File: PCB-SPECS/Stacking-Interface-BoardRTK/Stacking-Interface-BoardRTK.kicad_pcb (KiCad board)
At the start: 2 copper layers, 57 x 93 mm, 15 parts

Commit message: Really trying to get the PCB okay... will have to work on it tmr
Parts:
- RTK_Bottom_Left1: moved to B.Cu
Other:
- board size 57 x 93 mm -> 65 x 96 mm
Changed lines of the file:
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@@
 	)
 	(footprint "Connector_PinHeader_2.54mm:PinHeader_1x10_P2.54mm_Vertical"
-		(layer "F.Cu")
+		(layer "B.Cu")
 		(at 12 25.5 180)
 		(descr "Through hole straight pin header, 1x10, 2.54mm pitch, single row")
 		(tags "Through hole pin header THT 1x10 2.54mm single row")
 		(property "Reference" "RTK_Bottom_Left1"
-			(at 0 2.38 0)
-			(layer "B.SilkS")
+			(at 0 -2.38 0)
+			(layer "F.SilkS")
 			(effects
 				(font
-					(size 1 1)
-					(thickness 0.15)
+					(size 0.6 0.6)
+					(thickness 0.1)
 				)
-				(justify mirror)
 			)
 		)
 		(property "Value" "Conn_01x10_Pin"
-			(at 0 -25.24 0)
-			(layer "B.Fab")
+			(at 0 25.24 0)
+			(layer "F.Fab")
 			(effects
 				(font
@@
 					(thickness 0.15)
 				)
-				(justify mirror)
 			)
 		)
 		(property "Datasheet" "~"
 			(at 0 0 0)
-			(layer "B.Fab")
+			(layer "F.Fab")
 			(hide yes)
 			(effects
@@
 					(thickness 0.15)
 				)
-				(justify mirror)
 			)
 		)
 		(property "Description" "Generic connector, single row, 01x10, script generated"
 			(at 0 0 0)
-			(layer "B.Fab")
+			(layer "F.Fab")
 			(hide yes)
 			(effects
@@
 					(thickness 0.15)
 				)
-				(justify mirror)
 			)
 		)
@@
 				(type solid)
 			)
-			(layer "B.SilkS")
+			(layer "F.SilkS")
 		)
 		(fp_line
@@
 				(type solid)
 			)
-			(layer "B.SilkS")
+			(layer "F.SilkS")
 		)
 		(fp_line
@@
 				(type solid)
 			)
-			(layer "B.SilkS")
+			(layer "F.SilkS")
 		)
 		(fp_line
@@
 				(type solid)
 			)
-			(layer "B.SilkS")
+			(layer "F.SilkS")
 		)
 		(fp_line
@@
 				(type solid)
 			)
-			(layer "B.SilkS")
+			(layer "F.SilkS")
 		)
 		(fp_line
@@
 				(type solid)
 			)
-			(layer "B.SilkS")
+			(layer "F.SilkS")
 		)
 		(fp_line
@@
 				(type solid)
 			)
-			(layer "B.CrtYd")
+			(layer "F.CrtYd")
 		)
 		(fp_line
@@
 				(type solid)
 			)
-			(layer "B.CrtYd")
+			(layer "F.CrtYd")
 		)
 		(fp_line
@@
 				(type solid)
 			)
-			(layer "B.CrtYd")
+			(layer "F.CrtYd")
 		)
 		(fp_line
@@
 				(type solid)
 			)
-			(layer "B.CrtYd")
+			(layer "F.CrtYd")
 		)
 		(fp_line
@@
 		(model "${KICAD9_3DMODEL_DIR}/Connector_PinHeader_2.54mm.3dshapes/PinHeader_1x10_P2.54mm_Vertical.step"
 			(offset
-				(xyz 0 0 0)
+				(xyz 0 11.43 0)
 			)
 			(scale
@@
 			)
 			(rotate
-				(xyz 0 0 0)
+				(xyz 0 0 180)
 			)
 		)
@@
 		(tags "Through hole pin header THT 1x06 2.54mm single row")
 		(property "Reference" "RTK_Top_Right1"
-			(at 0 -2.38 0)
+			(at -14 -2.38 0)
 			(layer "F.SilkS")
 			(effects
 				(font
-					(size 1 1)
-					(thickness 0.15)
+					(size 0.6 0.6)
+					(thickness 0.1)
 				)
+				(justify right)
 			)
 		)
@@
 		(model "${KICAD9_3DMODEL_DIR}/Connector_PinHeader_2.54mm.3dshapes/PinHeader_1x06_P2.54mm_Vertical.step"
 			(offset
-				(xyz 0 0 0)
+				(xyz 0 0 -1.6)
 			)
 			(scale
@@
 			(effects
 				(font
-					(size 1 1)
-					(thickness 0.15)
+					(size 0.6 0.6)
+					(thickness 0.1)
 				)
 			)
@@
 		(model "${KICAD9_3DMODEL_DIR}/Connector_PinHeader_2.54mm.3dshapes/PinHeader_1x08_P2.54mm_Vertical.step"
 			(offset
-				(xyz 0 0 0)
+				(xyz 0 0 -1.6)
 			)
 			(scale
@@
 		(tags "Through hole pin header THT 1x08 2.54mm single row")
 		(property "Reference" "RTK_Bottom_Right1"
-			(at 0 -2.38 0)
+			(at -14 -2.38 0)
 			(layer "F.SilkS")
 			(effects
 				(font
-					(size 1 1)
-					(thickness 0.15)
+					(size 0.6 0.6)
+					(thickness 0.1)
 				)
+				(justify right)
 			)
 		)
@@
 		(model "${KICAD9_3DMODEL_DIR}/Connector_PinHeader_2.54mm.3dshapes/PinHeader_1x08_P2.54mm_Vertical.step"
 			(offset
-				(xyz 0 0 0)
+				(xyz 0 0 -1.6)
 			)
 			(scale
@@
 	)
 	(gr_rect
-		(start 6 1.5)
-		(end 63 94.5)
+		(start 2 0)
+		(end 67 96)
 		(stroke
 			(width 0.15)

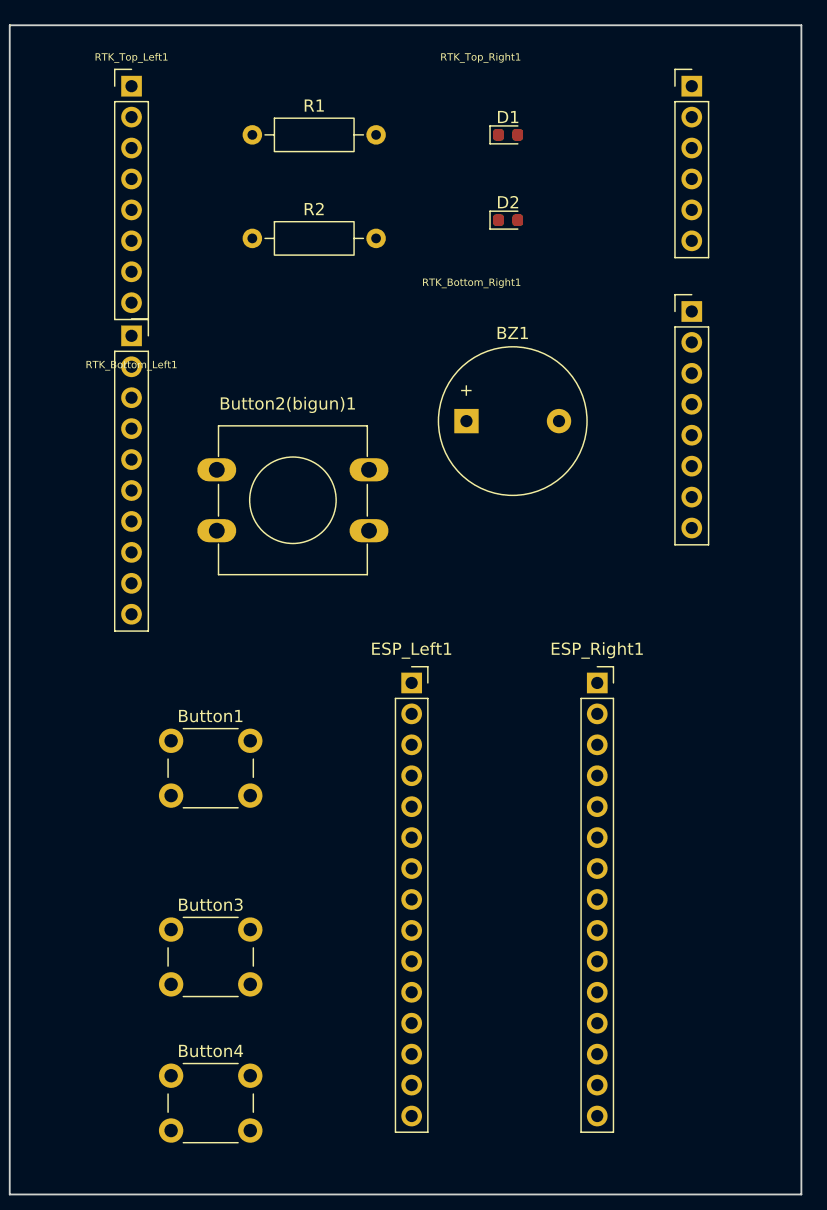
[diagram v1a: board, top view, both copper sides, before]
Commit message: Working on PCB, got the correct measurements for correct stacking with microcontroller elements
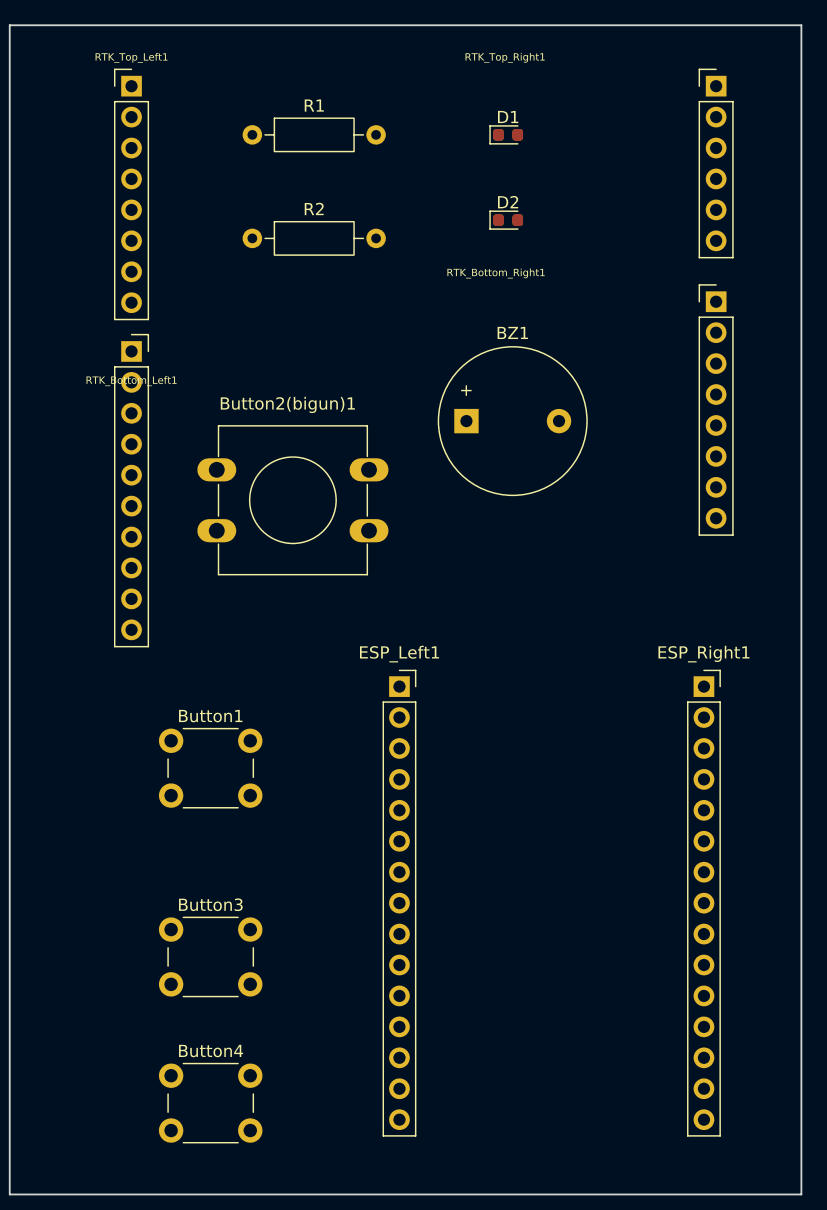
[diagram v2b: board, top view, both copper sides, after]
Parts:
- moved ESP_Right1 8.77 mm to (59.0, 54.3)
- moved RTK_Bottom_Right1 2.15 mm to (60.0, 22.7)
- moved RTK_Top_Right1 2.00 mm to (60.0, 5.00)
- moved RTK_Bottom_Left1 1.28 mm to (12.0, 26.8)
- moved ESP_Left1 1.04 mm to (34.0, 54.3)

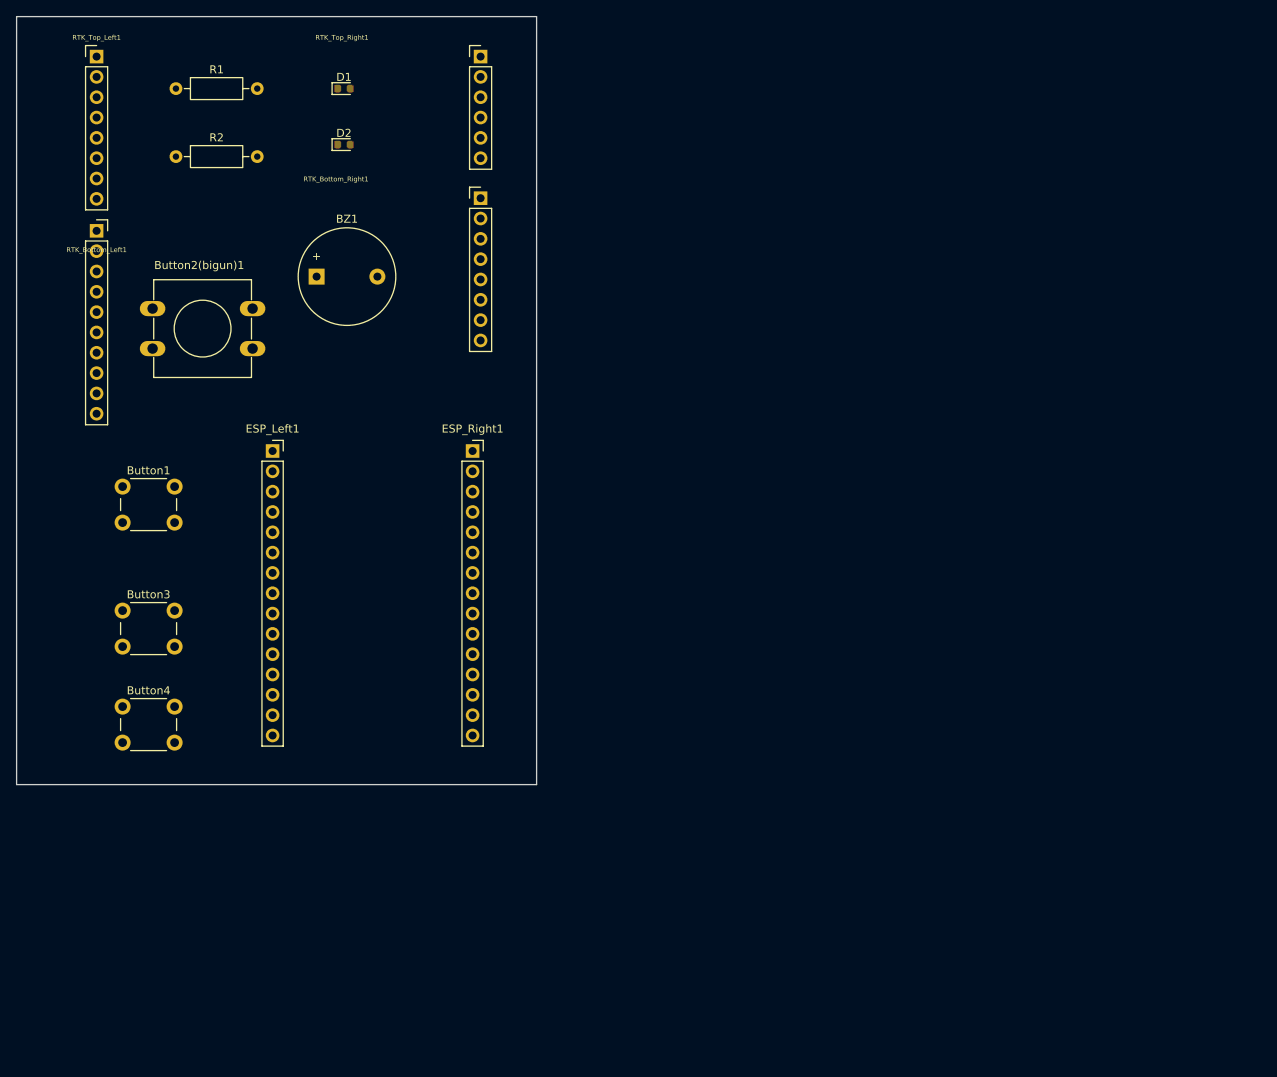
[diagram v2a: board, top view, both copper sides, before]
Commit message: updating pcb
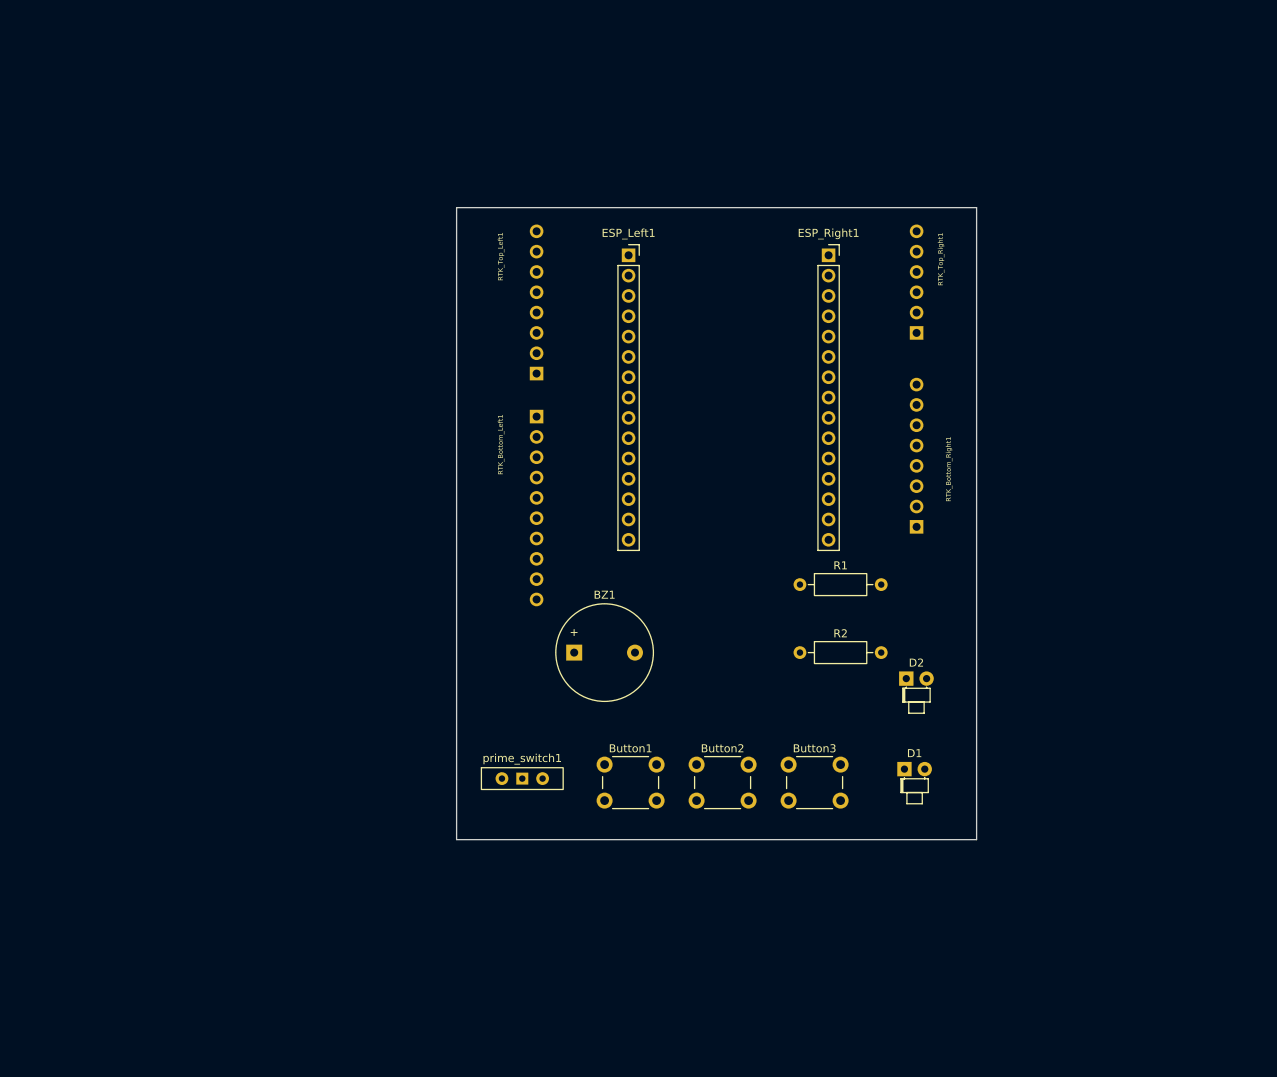
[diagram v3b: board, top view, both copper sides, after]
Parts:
- removed Button2(bigun)1: SW_Push, Button_Switch_THT:SW_PUSH-12mm
- added prime_switch1: SW_SPDT, Button_Switch_THT:SW_Slide-03_Wuerth-WS-SLTV_10x2.5x6.4_P2.54mm, F.Cu at (65.2, 95.2)
- D1, D2: footprint LED_SMD:LED_0603_1608Metric -> LED_THT:LED_D1.8mm_W1.8mm_H2.4mm_Horizontal_O1.27mm_Z1.6mm
- R1, R2: value R -> 1k
- moved D1 110.2 mm to (113.0, 94.1)
- moved R1 99.6 mm to (99.9, 71.0)
- moved R2 99.6 mm to (99.9, 79.5)
- moved D2 96.9 mm to (113.2, 82.8)
- moved Button3 83.6 mm to (98.5, 93.5)
- moved Button2 74.3 mm to (87.0, 93.5)
- moved Button1 69.6 mm to (75.5, 93.5)
- moved RTK_Bottom_Right1 68.2 mm to (114.5, 63.8)
- moved RTK_Top_Left1 67.8 mm to (67.0, 44.6)
- moved RTK_Top_Right1 64.5 mm to (114.5, 39.5)
- moved RTK_Bottom_Left1 59.7 mm to (67.0, 50.0)
- moved BZ1 57.0 mm to (71.7, 79.5)
- moved ESP_Left1 50.8 mm to (78.5, 29.8)
- moved ESP_Right1 50.8 mm to (103.5, 29.8)
- renumbered Button3 to Button2, Button4 to Button3
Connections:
- Button1 pad 1: Net-(ESP_Right1-Pin_2) -> Net-(ESP_Right1-Pin_1)
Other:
- board size 65 x 96 mm -> 65 x 79 mm

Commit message: pcb done
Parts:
- BZ1: footprint Buzzer_Beeper:Buzzer_12x9.5RM7.6 -> Buzzer_Beeper:Buzzer_D14mm_H7mm_P10mm
- moved prime_switch1 5.80 mm to (64.5, 101.0)
- moved Button1 5.00 mm to (75.5, 98.5)
- moved Button2 5.00 mm to (87.0, 98.5)
- moved Button3 5.00 mm to (98.5, 98.5)
- moved BZ1 3.50 mm to (73.5, 82.5)
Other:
- board size 65 x 79 mm -> 65 x 83 mm
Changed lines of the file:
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@@
 		)
 	)
-	(footprint "Buzzer_Beeper:Buzzer_12x9.5RM7.6"
+	(footprint "Buzzer_Beeper:Buzzer_D14mm_H7mm_P10mm"
 		(layer "F.Cu")
-		(at 71.7 79.5)
-		(descr "Generic Buzzer, D12mm height 9.5mm with RM7.6mm")
+		(at 73.5 82.5)
+		(descr "Generic Buzzer, D14mm height 7mm with pitch 10mm")
 		(tags "buzzer")
 		(property "Reference" "BZ1"
-			(at 3.8 -7.2 0)
+			(at 5.16 -8.23 0)
 			(layer "F.SilkS")
 			(effects
@@
 		)
 		(property "Value" "Buzzer"
-			(at 3.8 7.4 0)
+			(at 4.69 8.41 0)
 			(layer "F.Fab")
 			(effects
@@
 		(attr through_hole)
 		(fp_circle
-			(center 3.8 0)
-			(end 9.9 0)
+			(center 5 0)
+			(end 12.1 0)
 			(stroke
 				(width 0.12)
@@
 		)
 		(fp_circle
-			(center 3.8 0)
-			(end 10.05 0)
+			(center 5 0)
+			(end 12.25 0)
 			(stroke
 				(width 0.05)
@@
 		)
 		(fp_circle
-			(center 3.8 0)
-			(end 4.8 0)
+			(center 5 0)
+			(end 6 0)
 			(stroke
 				(width 0.1)
@@
 		)
 		(fp_circle
-			(center 3.8 0)
-			(end 9.8 0)
+			(center 5 0)
+			(end 12 0)
 			(stroke
 				(width 0.1)
@@
 		)
 		(fp_text user "${REFERENCE}"
-			(at 3.8 -4 0)
+			(at 5.32 2.27 0)
 			(layer "F.Fab")
 			(effects
@@
 		)
 		(pad "2" thru_hole circle
-			(at 7.6 0)
+			(at 10 0)
 			(size 2 2)
 			(drill 1)
@@
 		)
 		(embedded_fonts no)
-		(model "${KICAD9_3DMODEL_DIR}/Buzzer_Beeper.3dshapes/Buzzer_12x9.5RM7.6.step"
+		(model "${KICAD9_3DMODEL_DIR}/Buzzer_Beeper.3dshapes/Buzzer_D14mm_H7mm_P10mm.step"
 			(offset
 				(xyz 0 0 0)
@@
 	(footprint "Button_Switch_THT:SW_PUSH_6mm"
 		(layer "F.Cu")
-		(at 75.5 93.5)
+		(at 75.5 98.5)
 		(descr "Generic 6mm SW tactile push button")
 		(tags "tact sw push 6mm")
@@
 	(footprint "Button_Switch_THT:SW_Slide-03_Wuerth-WS-SLTV_10x2.5x6.4_P2.54mm"
 		(layer "F.Cu")
-		(at 65.21 95.25)
+		(at 64.46 101)
 		(descr "Wuerth, WS-SLTV, 450301014042, https://www.we-online.com/components/products/datasheet/450301014042.pdf")
 		(tags "switch single-pole opposite-side-connection double-throw SPDT würth wurth")
@@
 	(footprint "Button_Switch_THT:SW_PUSH_6mm"
 		(layer "F.Cu")
-		(at 87 93.5)
+		(at 87 98.5)
 		(descr "Generic 6mm SW tactile push button")
 		(tags "tact sw push 6mm")
@@
 	(footprint "Button_Switch_THT:SW_PUSH_6mm"
 		(layer "F.Cu")
-		(at 98.5 93.5)
+		(at 98.5 98.5)
 		(descr "Generic 6mm SW tactile push button")
 		(tags "tact sw push 6mm")
@@
 	(gr_rect
 		(start 57 23.88)
-		(end 122 102.88)
+		(end 122 106.88)
 		(stroke
 			(width 0.15)

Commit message: finished designing pcb
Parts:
- removed Button3: SW_Push, Button_Switch_THT:SW_PUSH_6mm
- added G***: LOGO, graphics:watermelon, F.Cu at (117.0, 108.0)
- added J1: Screw_Terminal_01x02, TerminalBlock:TerminalBlock_Altech_AK300-2_P5.00mm, F.Cu at (138.0, 122.5)
- added hole1: MountingHole_3.2mm_M3, MountingHole:MountingHole_3.2mm_M3, F.Cu at (96.0, 54.0)
- added hole2: MountingHole_3.2mm_M3, MountingHole:MountingHole_3.2mm_M3, F.Cu at (152.5, 54.0)
- added hole3: MountingHole_3.2mm_M3, MountingHole:MountingHole_3.2mm_M3, F.Cu at (153.0, 126.0)
- added kibuzzard-69A9F479: G***, kibuzzard-69A9F479, F.Cu at (124.0, 54.0)
- prime_switch1: footprint Button_Switch_THT:SW_Slide-03_Wuerth-WS-SLTV_10x2.5x6.4_P2.54mm -> watermelonstuff:spdt_switch
- moved prime_switch1 73.1 mm to (137.0, 110.0)
- moved RTK_Bottom_Left1 45.2 mm to (99.5, 81.5)
- moved D2 45.2 mm to (150.2, 108.7), turned to -90 degrees
- moved ESP_Left1 44.8 mm to (111.0, 60.7)
- moved ESP_Right1 44.8 mm to (136.0, 60.7)
- moved BZ1 44.3 mm to (95.5, 121.0)
- moved Button1 43.7 mm to (113.5, 120.0)
- moved Button2 43.2 mm to (124.5, 120.0)
- moved RTK_Top_Right1 38.5 mm to (147.5, 59.5), turned to 180 degrees
- moved D1 37.9 mm to (150.2, 101.2), turned to -90 degrees
- moved RTK_Top_Left1 35.7 mm to (99.5, 59.5), turned to 180 degrees
- moved RTK_Bottom_Right1 35.5 mm to (147.5, 77.0), turned to 180 degrees
- moved R2 22.7 mm to (118.5, 66.5)
- moved R1 21.6 mm to (118.5, 60.0)
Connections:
- ESP_Left1 pad 15: unconnected-(ESP_Left1-Pin_15-Pad15) -> VCC
- RTK_Bottom_Right1 pad 1: GND -> unconnected-(RTK_Bottom_Right1-Pin_1-Pad1)
- RTK_Bottom_Right1 pad 3: unconnected-(RTK_Bottom_Right1-Pin_3-Pad3) -> GND
- RTK_Bottom_Right1 pad 4: unconnected-(RTK_Bottom_Right1-Pin_4-Pad4) -> VCC
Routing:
- net GND: track 0.00 -> 102.0 mm
- net Net-(ESP_Right1-Pin_10): track 0.00 -> 91.8 mm, vias 0 -> 2
- net Net-(BZ1-+): track 0.00 -> 84.6 mm, vias 0 -> 1
- net Net-(BZ1--): track 0.00 -> 76.7 mm, vias 0 -> 1
- net Net-(ESP_Right1-Pin_1): track 0.00 -> 74.3 mm
- net Net-(D2-A): track 0.00 -> 72.5 mm, vias 0 -> 1
- net Net-(D1-A): track 0.00 -> 61.6 mm, vias 0 -> 1
- net Net-(ESP_Right1-Pin_6): track 0.00 -> 55.2 mm
- net Net-(ESP_Right1-Pin_2): track 0.00 -> 50.6 mm
- net Net-(ESP_Right1-Pin_7): track 0.00 -> 50.2 mm
- net VCC: track 0.00 -> 41.3 mm
- net Net-(ESP_Left1-Pin_5): track 0.00 -> 14.0 mm
- net Net-(ESP_Left1-Pin_6): track 0.00 -> 10.4 mm
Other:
- board size 65 x 83 mm -> 66.5 x 81.5 mm
- board text added: "03/05/2026"
- board text added: "Garden E-Cutters: Mid Layer PCB"
- board text added: "J.A. M.J.M. C.V. A.F.M. A.G."
